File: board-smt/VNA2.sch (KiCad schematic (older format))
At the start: 61 parts, among them U2 LM339, U3 SA612, U4 SA612, U5 SA612, U6 LM358, U7 LM358

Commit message: Changed SMA connector, added dual power option for LCD
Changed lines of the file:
@@
 LIBS:sa612
 LIBS:si5351a
+LIBS:AMS1117-3V3
 LIBS:VNA-cache
 EELAYER 25 0
@@
 $EndComp
 $Comp
-L GND #PWR046
+L GND #PWR59
 U 1 1 5BB32DBE
 P 3150 950
-F 0 "#PWR046" H 3150 700 50  0001 C CNN
+F 0 "#PWR59" H 3150 700 50  0001 C CNN
 F 1 "GND" H 3150 800 50  0000 C CNN
 F 2 "" H 3150 950 50  0001 C CNN
@@
 $EndComp
 $Comp
-L GND #PWR047
+L GND #PWR50
 U 1 1 5BB32DD3
 P 1100 1700
-F 0 "#PWR047" H 1100 1450 50  0001 C CNN
+F 0 "#PWR50" H 1100 1450 50  0001 C CNN
 F 1 "GND" H 1100 1550 50  0000 C CNN
 F 2 "" H 1100 1700 50  0001 C CNN
@@
 $EndComp
 $Comp
-L GND #PWR048
+L GND #PWR53
 U 1 1 5BB32DD9
 P 1500 1800
-F 0 "#PWR048" H 1500 1550 50  0001 C CNN
+F 0 "#PWR53" H 1500 1550 50  0001 C CNN
 F 1 "GND" H 1500 1650 50  0000 C CNN
 F 2 "" H 1500 1800 50  0001 C CNN
@@
 $EndComp
 $Comp
-L GND #PWR049
+L GND #PWR56
 U 1 1 5BB32DF0
 P 1900 2250
-F 0 "#PWR049" H 1900 2000 50  0001 C CNN
+F 0 "#PWR56" H 1900 2000 50  0001 C CNN
 F 1 "GND" H 1900 2100 50  0000 C CNN
 F 2 "" H 1900 2250 50  0001 C CNN
@@
 $EndComp
 $Comp
-L GND #PWR050
+L GND #PWR61
 U 1 1 5BB32E0B
 P 4350 2450
-F 0 "#PWR050" H 4350 2200 50  0001 C CNN
+F 0 "#PWR61" H 4350 2200 50  0001 C CNN
 F 1 "GND" H 4350 2300 50  0000 C CNN
 F 2 "" H 4350 2450 50  0001 C CNN
@@
 FILT5V
 $Comp
-L GND #PWR051
+L GND #PWR63
 U 1 1 5BB32E19
 P 4650 1800
-F 0 "#PWR051" H 4650 1550 50  0001 C CNN
+F 0 "#PWR63" H 4650 1550 50  0001 C CNN
 F 1 "GND" H 4650 1650 50  0000 C CNN
 F 2 "" H 4650 1800 50  0001 C CNN
@@
 $EndComp
 $Comp
-L GND #PWR052
+L GND #PWR58
 U 1 1 5BB32E52
 P 3100 2750
-F 0 "#PWR052" H 3100 2500 50  0001 C CNN
+F 0 "#PWR58" H 3100 2500 50  0001 C CNN
 F 1 "GND" H 3100 2600 50  0000 C CNN
 F 2 "" H 3100 2750 50  0001 C CNN
@@
 $EndComp
 $Comp
-L GND #PWR053
+L GND #PWR49
 U 1 1 5BB32E67
 P 1050 3500
-F 0 "#PWR053" H 1050 3250 50  0001 C CNN
+F 0 "#PWR49" H 1050 3250 50  0001 C CNN
 F 1 "GND" H 1050 3350 50  0000 C CNN
 F 2 "" H 1050 3500 50  0001 C CNN
@@
 $EndComp
 $Comp
-L GND #PWR054
+L GND #PWR52
 U 1 1 5BB32E6D
 P 1450 3600
-F 0 "#PWR054" H 1450 3350 50  0001 C CNN
+F 0 "#PWR52" H 1450 3350 50  0001 C CNN
 F 1 "GND" H 1450 3450 50  0000 C CNN
 F 2 "" H 1450 3600 50  0001 C CNN
@@
 $EndComp
 $Comp
-L GND #PWR055
+L GND #PWR55
 U 1 1 5BB32E84
 P 1850 4050
-F 0 "#PWR055" H 1850 3800 50  0001 C CNN
+F 0 "#PWR55" H 1850 3800 50  0001 C CNN
 F 1 "GND" H 1850 3900 50  0000 C CNN
 F 2 "" H 1850 4050 50  0001 C CNN
@@
 $EndComp
 $Comp
-L GND #PWR056
+L GND #PWR65
 U 1 1 5BB32ED8
 P 5700 2600
-F 0 "#PWR056" H 5700 2350 50  0001 C CNN
+F 0 "#PWR65" H 5700 2350 50  0001 C CNN
 F 1 "GND" H 5700 2450 50  0000 C CNN
 F 2 "" H 5700 2600 50  0001 C CNN
@@
 $EndComp
 $Comp
-L GND #PWR057
+L GND #PWR67
 U 1 1 5BB32EE5
 P 6000 2600
-F 0 "#PWR057" H 6000 2350 50  0001 C CNN
+F 0 "#PWR67" H 6000 2350 50  0001 C CNN
 F 1 "GND" H 6000 2450 50  0000 C CNN
 F 2 "" H 6000 2600 50  0001 C CNN
@@
 $EndComp
 $Comp
-L GND #PWR058
+L GND #PWR69
 U 1 1 5BB32EFA
 P 6200 3650
-F 0 "#PWR058" H 6200 3400 50  0001 C CNN
+F 0 "#PWR69" H 6200 3400 50  0001 C CNN
 F 1 "GND" H 6200 3500 50  0000 C CNN
 F 2 "" H 6200 3650 50  0001 C CNN
@@
 $EndComp
 $Comp
-L GND #PWR059
+L GND #PWR70
 U 1 1 5BB32F07
 P 6500 3650
-F 0 "#PWR059" H 6500 3400 50  0001 C CNN
+F 0 "#PWR70" H 6500 3400 50  0001 C CNN
 F 1 "GND" H 6500 3500 50  0000 C CNN
 F 2 "" H 6500 3650 50  0001 C CNN
@@
 $EndComp
 $Comp
-L GND #PWR060
+L GND #PWR60
 U 1 1 5BB496C5
 P 3300 4800
-F 0 "#PWR060" H 3300 4550 50  0001 C CNN
+F 0 "#PWR60" H 3300 4550 50  0001 C CNN
 F 1 "GND" H 3300 4650 50  0000 C CNN
 F 2 "" H 3300 4800 50  0001 C CNN
@@
 $EndComp
 $Comp
-L GND #PWR061
+L GND #PWR51
 U 1 1 5BB496D8
 P 1250 5550
-F 0 "#PWR061" H 1250 5300 50  0001 C CNN
+F 0 "#PWR51" H 1250 5300 50  0001 C CNN
 F 1 "GND" H 1250 5400 50  0000 C CNN
 F 2 "" H 1250 5550 50  0001 C CNN
@@
 $EndComp
 $Comp
-L GND #PWR062
+L GND #PWR54
 U 1 1 5BB496DE
 P 1650 5650
-F 0 "#PWR062" H 1650 5400 50  0001 C CNN
+F 0 "#PWR54" H 1650 5400 50  0001 C CNN
 F 1 "GND" H 1650 5500 50  0000 C CNN
 F 2 "" H 1650 5650 50  0001 C CNN
@@
 $EndComp
 $Comp
-L GND #PWR063
+L GND #PWR57
 U 1 1 5BB496F3
 P 2050 6100
-F 0 "#PWR063" H 2050 5850 50  0001 C CNN
+F 0 "#PWR57" H 2050 5850 50  0001 C CNN
 F 1 "GND" H 2050 5950 50  0000 C CNN
 F 2 "" H 2050 6100 50  0001 C CNN
@@
 $EndComp
 $Comp
-L GND #PWR064
+L GND #PWR62
 U 1 1 5BB4970B
 P 4500 6300
-F 0 "#PWR064" H 4500 6050 50  0001 C CNN
+F 0 "#PWR62" H 4500 6050 50  0001 C CNN
 F 1 "GND" H 4500 6150 50  0000 C CNN
 F 2 "" H 4500 6300 50  0001 C CNN
@@
 FILT5V
 $Comp
-L GND #PWR065
+L GND #PWR64
 U 1 1 5BB49718
 P 4800 5650
-F 0 "#PWR065" H 4800 5400 50  0001 C CNN
+F 0 "#PWR64" H 4800 5400 50  0001 C CNN
 F 1 "GND" H 4800 5500 50  0000 C CNN
 F 2 "" H 4800 5650 50  0001 C CNN
@@
 $EndComp
 $Comp
-L GND #PWR066
+L GND #PWR66
 U 1 1 5BB4974C
 P 5850 6450
-F 0 "#PWR066" H 5850 6200 50  0001 C CNN
+F 0 "#PWR66" H 5850 6200 50  0001 C CNN
 F 1 "GND" H 5850 6300 50  0000 C CNN
 F 2 "" H 5850 6450 50  0001 C CNN
@@
 $EndComp
 $Comp
-L GND #PWR067
+L GND #PWR68
 U 1 1 5BB49758
 P 6150 6450
-F 0 "#PWR067" H 6150 6200 50  0001 C CNN
+F 0 "#PWR68" H 6150 6200 50  0001 C CNN
 F 1 "GND" H 6150 6300 50  0000 C CNN
 F 2 "" H 6150 6450 50  0001 C CNN
@@
 $EndComp
 $Comp
-L GND #PWR068
+L GND #PWR71
 U 1 1 5BB4F877
 P 6700 1650
-F 0 "#PWR068" H 6700 1400 50  0001 C CNN
+F 0 "#PWR71" H 6700 1400 50  0001 C CNN
 F 1 "GND" H 6700 1500 50  0000 C CNN
 F 2 "" H 6700 1650 50  0001 C CNN
@@
 $EndComp
 $Comp
-L GND #PWR069
+L GND #PWR73
 U 1 1 5BF2333C
 P 8550 850
-F 0 "#PWR069" H 8550 600 50  0001 C CNN
+F 0 "#PWR73" H 8550 600 50  0001 C CNN
 F 1 "GND" H 8550 700 50  0000 C CNN
 F 2 "" H 8550 850 50  0001 C CNN
@@
 $EndComp
 $Comp
-L GND #PWR070
+L GND #PWR75
 U 1 1 5BF23614
 P 8850 2000
-F 0 "#PWR070" H 8850 1750 50  0001 C CNN
+F 0 "#PWR75" H 8850 1750 50  0001 C CNN
 F 1 "GND" H 8850 1850 50  0000 C CNN
 F 2 "" H 8850 2000 50  0001 C CNN
@@
 $EndComp
 $Comp
-L GND #PWR071
+L GND #PWR74
 U 1 1 5BF238FB
 P 8550 1900
-F 0 "#PWR071" H 8550 1650 50  0001 C CNN
+F 0 "#PWR74" H 8550 1650 50  0001 C CNN
 F 1 "GND" H 8550 1750 50  0000 C CNN
 F 2 "" H 8550 1900 50  0001 C CNN
@@
 FILT5V
 $Comp
-L GND #PWR072
+L GND #PWR72
 U 1 1 5BF23F5D
 P 8500 2800
-F 0 "#PWR072" H 8500 2550 50  0001 C CNN
+F 0 "#PWR72" H 8500 2550 50  0001 C CNN
 F 1 "GND" H 8500 2650 50  0000 C CNN
 F 2 "" H 8500 2800 50  0001 C CNN
@@
 	1800 5500 1800 5800
 Wire Wire Line
-	3250 5400 3400 5400
+	3400 5400 3250 5400
 Wire Wire Line
 	3050 5400 2950 5400
@@
 	1600 3450 1600 3750
 Wire Wire Line
-	3050 3350 3200 3350
+	3200 3350 3050 3350
 Wire Wire Line
 	2850 3350 2750 3350
@@
 	1650 1650 1650 1950
 Wire Wire Line
-	3100 1550 3250 1550
+	3250 1550 3100 1550
 Wire Wire Line
 	2900 1550 2800 1550

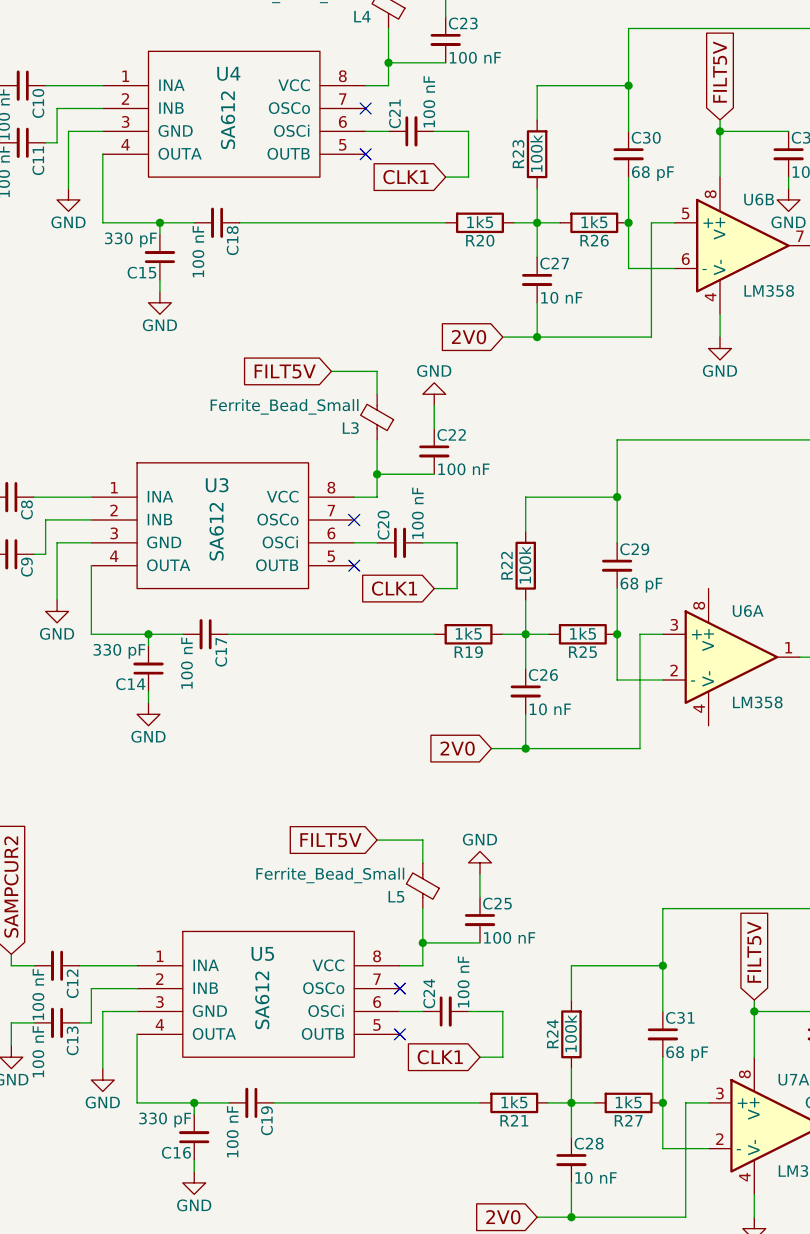
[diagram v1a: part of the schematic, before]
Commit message: Increased isolation between ports
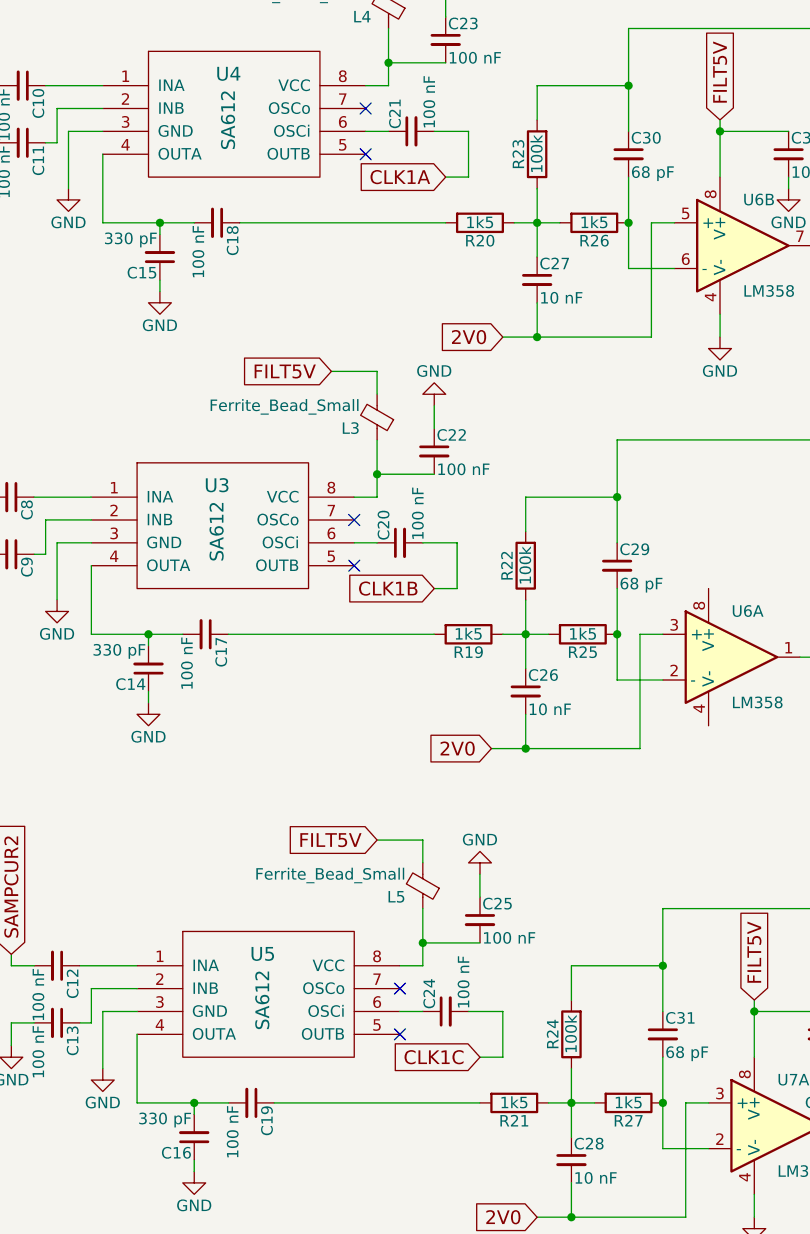
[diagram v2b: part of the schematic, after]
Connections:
- removed net CLK1: C20.2, C21.2, C24.2
- new net CLK1A: C21.2
- new net CLK1B: C20.2
- new net CLK1C: C24.2
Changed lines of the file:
@@
 $EndComp
 $Comp
-L GND #PWR59
+L GND #PWR61
 U 1 1 5BB32DBE
 P 3150 950
-F 0 "#PWR59" H 3150 700 50  0001 C CNN
+F 0 "#PWR61" H 3150 700 50  0001 C CNN
 F 1 "GND" H 3150 800 50  0000 C CNN
 F 2 "" H 3150 950 50  0001 C CNN
@@
 $EndComp
 $Comp
-L GND #PWR50
+L GND #PWR52
 U 1 1 5BB32DD3
 P 1100 1700
-F 0 "#PWR50" H 1100 1450 50  0001 C CNN
+F 0 "#PWR52" H 1100 1450 50  0001 C CNN
 F 1 "GND" H 1100 1550 50  0000 C CNN
 F 2 "" H 1100 1700 50  0001 C CNN
@@
 $EndComp
 $Comp
-L GND #PWR53
+L GND #PWR55
 U 1 1 5BB32DD9
 P 1500 1800
-F 0 "#PWR53" H 1500 1550 50  0001 C CNN
+F 0 "#PWR55" H 1500 1550 50  0001 C CNN
 F 1 "GND" H 1500 1650 50  0000 C CNN
 F 2 "" H 1500 1800 50  0001 C CNN
@@
 NoConn ~ 2800 1450
 Text GLabel 3150 1750 0    60   Input ~ 0
-CLK1
+CLK1A
 $Comp
 L C_Small C21
@@
 $EndComp
 $Comp
-L GND #PWR56
+L GND #PWR58
 U 1 1 5BB32DF0
 P 1900 2250
-F 0 "#PWR56" H 1900 2000 50  0001 C CNN
+F 0 "#PWR58" H 1900 2000 50  0001 C CNN
 F 1 "GND" H 1900 2100 50  0000 C CNN
 F 2 "" H 1900 2250 50  0001 C CNN
@@
 $EndComp
 $Comp
-L GND #PWR61
+L GND #PWR63
 U 1 1 5BB32E0B
 P 4350 2450
-F 0 "#PWR61" H 4350 2200 50  0001 C CNN
+F 0 "#PWR63" H 4350 2200 50  0001 C CNN
 F 1 "GND" H 4350 2300 50  0000 C CNN
 F 2 "" H 4350 2450 50  0001 C CNN
@@
 FILT5V
 $Comp
-L GND #PWR63
+L GND #PWR65
 U 1 1 5BB32E19
 P 4650 1800
-F 0 "#PWR63" H 4650 1550 50  0001 C CNN
+F 0 "#PWR65" H 4650 1550 50  0001 C CNN
 F 1 "GND" H 4650 1650 50  0000 C CNN
 F 2 "" H 4650 1800 50  0001 C CNN
@@
 $EndComp
 $Comp
-L GND #PWR58
+L GND #PWR60
 U 1 1 5BB32E52
 P 3100 2750
-F 0 "#PWR58" H 3100 2500 50  0001 C CNN
+F 0 "#PWR60" H 3100 2500 50  0001 C CNN
 F 1 "GND" H 3100 2600 50  0000 C CNN
 F 2 "" H 3100 2750 50  0001 C CNN
@@
 $EndComp
 $Comp
-L GND #PWR49
+L GND #PWR51
 U 1 1 5BB32E67
 P 1050 3500
-F 0 "#PWR49" H 1050 3250 50  0001 C CNN
+F 0 "#PWR51" H 1050 3250 50  0001 C CNN
 F 1 "GND" H 1050 3350 50  0000 C CNN
 F 2 "" H 1050 3500 50  0001 C CNN
@@
 $EndComp
 $Comp
-L GND #PWR52
+L GND #PWR54
 U 1 1 5BB32E6D
 P 1450 3600
-F 0 "#PWR52" H 1450 3350 50  0001 C CNN
+F 0 "#PWR54" H 1450 3350 50  0001 C CNN
 F 1 "GND" H 1450 3450 50  0000 C CNN
 F 2 "" H 1450 3600 50  0001 C CNN
@@
 NoConn ~ 2750 3250
 Text GLabel 3100 3550 0    60   Input ~ 0
-CLK1
+CLK1B
 $Comp
 L C_Small C20
@@
 $EndComp
 $Comp
-L GND #PWR55
+L GND #PWR57
 U 1 1 5BB32E84
 P 1850 4050
-F 0 "#PWR55" H 1850 3800 50  0001 C CNN
+F 0 "#PWR57" H 1850 3800 50  0001 C CNN
 F 1 "GND" H 1850 3900 50  0000 C CNN
 F 2 "" H 1850 4050 50  0001 C CNN
@@
 $EndComp
 $Comp
-L GND #PWR65
+L GND #PWR67
 U 1 1 5BB32ED8
 P 5700 2600
-F 0 "#PWR65" H 5700 2350 50  0001 C CNN
+F 0 "#PWR67" H 5700 2350 50  0001 C CNN
 F 1 "GND" H 5700 2450 50  0000 C CNN
 F 2 "" H 5700 2600 50  0001 C CNN
@@
 $EndComp
 $Comp
-L GND #PWR67
+L GND #PWR69
 U 1 1 5BB32EE5
 P 6000 2600
-F 0 "#PWR67" H 6000 2350 50  0001 C CNN
+F 0 "#PWR69" H 6000 2350 50  0001 C CNN
 F 1 "GND" H 6000 2450 50  0000 C CNN
 F 2 "" H 6000 2600 50  0001 C CNN
@@
 $EndComp
 $Comp
-L GND #PWR69
+L GND #PWR71
 U 1 1 5BB32EFA
 P 6200 3650
-F 0 "#PWR69" H 6200 3400 50  0001 C CNN
+F 0 "#PWR71" H 6200 3400 50  0001 C CNN
 F 1 "GND" H 6200 3500 50  0000 C CNN
 F 2 "" H 6200 3650 50  0001 C CNN
@@
 $EndComp
 $Comp
-L GND #PWR70
+L GND #PWR72
 U 1 1 5BB32F07
 P 6500 3650
-F 0 "#PWR70" H 6500 3400 50  0001 C CNN
+F 0 "#PWR72" H 6500 3400 50  0001 C CNN
 F 1 "GND" H 6500 3500 50  0000 C CNN
 F 2 "" H 6500 3650 50  0001 C CNN
@@
 $EndComp
 $Comp
-L GND #PWR60
+L GND #PWR62
 U 1 1 5BB496C5
 P 3300 4800
-F 0 "#PWR60" H 3300 4550 50  0001 C CNN
+F 0 "#PWR62" H 3300 4550 50  0001 C CNN
 F 1 "GND" H 3300 4650 50  0000 C CNN
 F 2 "" H 3300 4800 50  0001 C CNN
@@
 $EndComp
 $Comp
-L GND #PWR51
+L GND #PWR53
 U 1 1 5BB496D8
 P 1250 5550
-F 0 "#PWR51" H 1250 5300 50  0001 C CNN
+F 0 "#PWR53" H 1250 5300 50  0001 C CNN
 F 1 "GND" H 1250 5400 50  0000 C CNN
 F 2 "" H 1250 5550 50  0001 C CNN
@@
 $EndComp
 $Comp
-L GND #PWR54
+L GND #PWR56
 U 1 1 5BB496DE
 P 1650 5650
-F 0 "#PWR54" H 1650 5400 50  0001 C CNN
+F 0 "#PWR56" H 1650 5400 50  0001 C CNN
 F 1 "GND" H 1650 5500 50  0000 C CNN
 F 2 "" H 1650 5650 50  0001 C CNN
@@
 NoConn ~ 2950 5300
 Text GLabel 3300 5600 0    60   Input ~ 0
-CLK1
+CLK1C
 $Comp
 L C_Small C24
@@
 $EndComp
 $Comp
-L GND #PWR57
+L GND #PWR59
 U 1 1 5BB496F3
 P 2050 6100
-F 0 "#PWR57" H 2050 5850 50  0001 C CNN
+F 0 "#PWR59" H 2050 5850 50  0001 C CNN
 F 1 "GND" H 2050 5950 50  0000 C CNN
 F 2 "" H 2050 6100 50  0001 C CNN
@@
 $EndComp
 $Comp
-L GND #PWR62
+L GND #PWR64
 U 1 1 5BB4970B
 P 4500 6300
-F 0 "#PWR62" H 4500 6050 50  0001 C CNN
+F 0 "#PWR64" H 4500 6050 50  0001 C CNN
 F 1 "GND" H 4500 6150 50  0000 C CNN
 F 2 "" H 4500 6300 50  0001 C CNN
@@
 FILT5V
 $Comp
-L GND #PWR64
+L GND #PWR66
 U 1 1 5BB49718
 P 4800 5650
-F 0 "#PWR64" H 4800 5400 50  0001 C CNN
+F 0 "#PWR66" H 4800 5400 50  0001 C CNN
 F 1 "GND" H 4800 5500 50  0000 C CNN
 F 2 "" H 4800 5650 50  0001 C CNN
@@
 $EndComp
 $Comp
-L GND #PWR66
+L GND #PWR68
 U 1 1 5BB4974C
 P 5850 6450
-F 0 "#PWR66" H 5850 6200 50  0001 C CNN
+F 0 "#PWR68" H 5850 6200 50  0001 C CNN
 F 1 "GND" H 5850 6300 50  0000 C CNN
 F 2 "" H 5850 6450 50  0001 C CNN
@@
 $EndComp
 $Comp
-L GND #PWR68
+L GND #PWR70
 U 1 1 5BB49758
 P 6150 6450
-F 0 "#PWR68" H 6150 6200 50  0001 C CNN
+F 0 "#PWR70" H 6150 6200 50  0001 C CNN
 F 1 "GND" H 6150 6300 50  0000 C CNN
 F 2 "" H 6150 6450 50  0001 C CNN
@@
 $EndComp
 $Comp
-L GND #PWR71
+L GND #PWR73
 U 1 1 5BB4F877
 P 6700 1650
-F 0 "#PWR71" H 6700 1400 50  0001 C CNN
+F 0 "#PWR73" H 6700 1400 50  0001 C CNN
 F 1 "GND" H 6700 1500 50  0000 C CNN
 F 2 "" H 6700 1650 50  0001 C CNN
@@
 $EndComp
 $Comp
-L GND #PWR73
+L GND #PWR75
 U 1 1 5BF2333C
 P 8550 850
-F 0 "#PWR73" H 8550 600 50  0001 C CNN
+F 0 "#PWR75" H 8550 600 50  0001 C CNN
 F 1 "GND" H 8550 700 50  0000 C CNN
 F 2 "" H 8550 850 50  0001 C CNN
@@
 $EndComp
 $Comp
-L GND #PWR75
+L GND #PWR77
 U 1 1 5BF23614
 P 8850 2000
-F 0 "#PWR75" H 8850 1750 50  0001 C CNN
+F 0 "#PWR77" H 8850 1750 50  0001 C CNN
 F 1 "GND" H 8850 1850 50  0000 C CNN
 F 2 "" H 8850 2000 50  0001 C CNN
@@
 $EndComp
 $Comp
-L GND #PWR74
+L GND #PWR76
 U 1 1 5BF238FB
 P 8550 1900
-F 0 "#PWR74" H 8550 1650 50  0001 C CNN
+F 0 "#PWR76" H 8550 1650 50  0001 C CNN
 F 1 "GND" H 8550 1750 50  0000 C CNN
 F 2 "" H 8550 1900 50  0001 C CNN
@@
 FILT5V
 $Comp
-L GND #PWR72
+L GND #PWR74
 U 1 1 5BF23F5D
 P 8500 2800
-F 0 "#PWR72" H 8500 2550 50  0001 C CNN
+F 0 "#PWR74" H 8500 2550 50  0001 C CNN
 F 1 "GND" H 8500 2650 50  0000 C CNN
 F 2 "" H 8500 2800 50  0001 C CNN
